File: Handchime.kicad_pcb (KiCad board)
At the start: 4 copper layers, 40.6 x 20.2 mm, 23 parts, among them J1 USB_C_Receptacle_USB2.0_16P, J2 Pins, J3 SWD, SW0 BOOT, SW1 Row 0, Col 0, SW2 Row 0, Col 1, U1 STM32C071GBUx, U2 PRTR5V0U2X, U3 XC6206P332MR-G

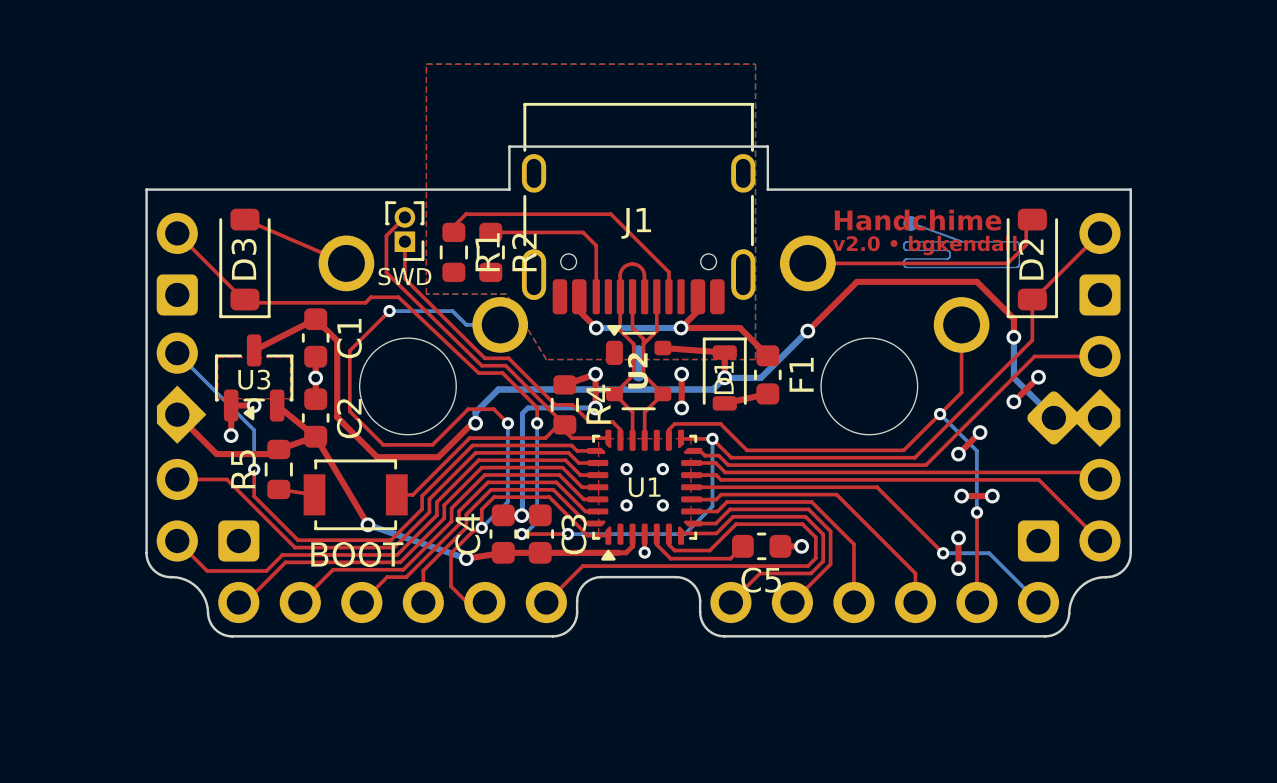
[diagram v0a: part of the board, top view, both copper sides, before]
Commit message: Clean-up edge cuts, tidy routing around NRST
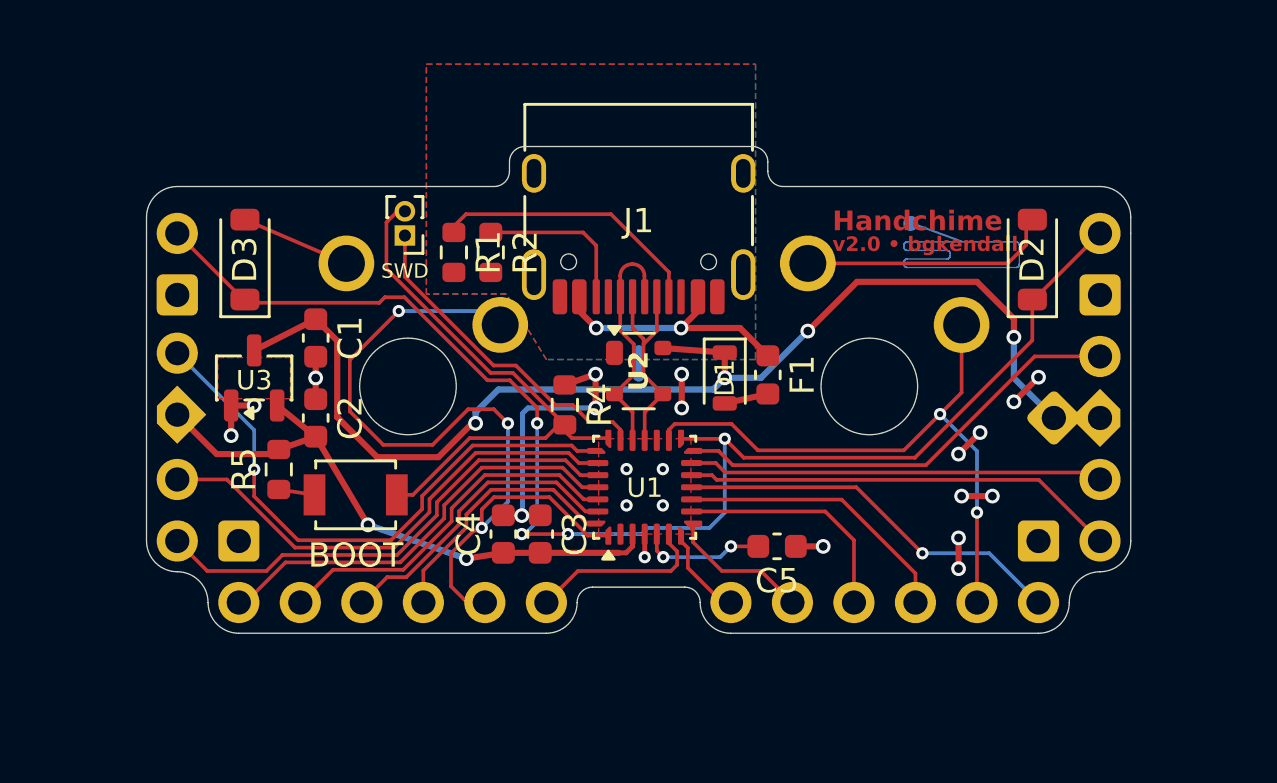
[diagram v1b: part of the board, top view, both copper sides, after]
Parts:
- moved C5 0.64 mm to (158.1, 57.4)
- moved J3 0.25 mm to (142.7, 44.6)
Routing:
- net PA0: track 20.0 -> 7.45 mm
- net PA1: track 12.1 -> 3.82 mm
- net PA2: track 9.89 -> 5.90 mm
- net NRST: track 4.44 -> 5.17 mm, vias 0 -> 2
- net R0: track 57.1 -> 57.8 mm
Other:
- board size 40.6 x 20.2 mm -> 40.6 x 16.5 mm

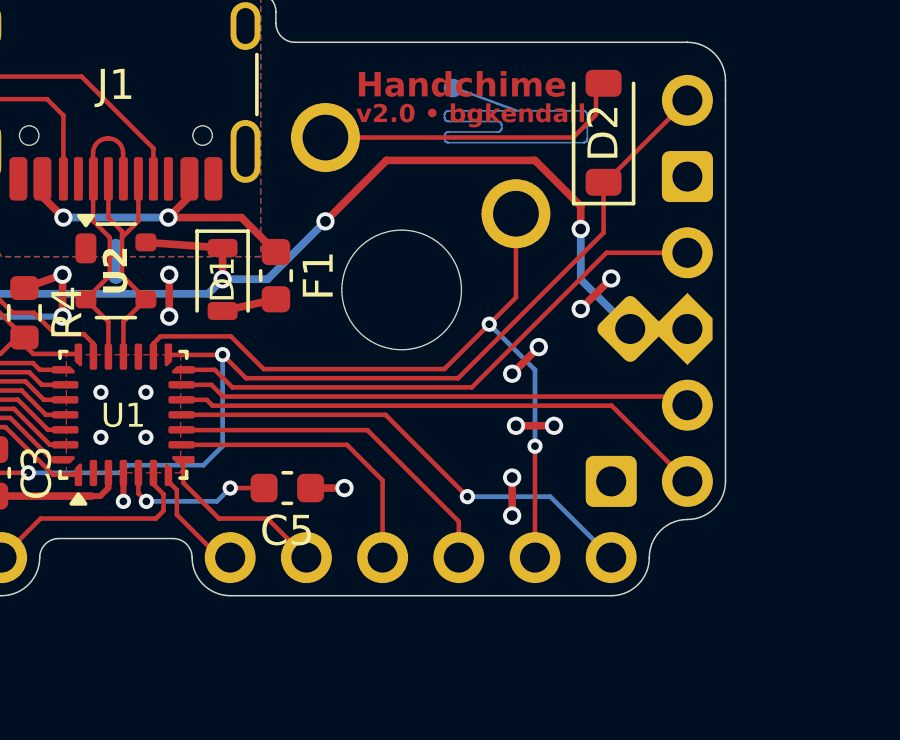
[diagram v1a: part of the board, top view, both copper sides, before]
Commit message: Add RGB pull-up to edge pin 22
PB0 has the following timers available for driving RGB LEDs using PWM:

 * TIM3_CH3
 * TIM1_CH2N
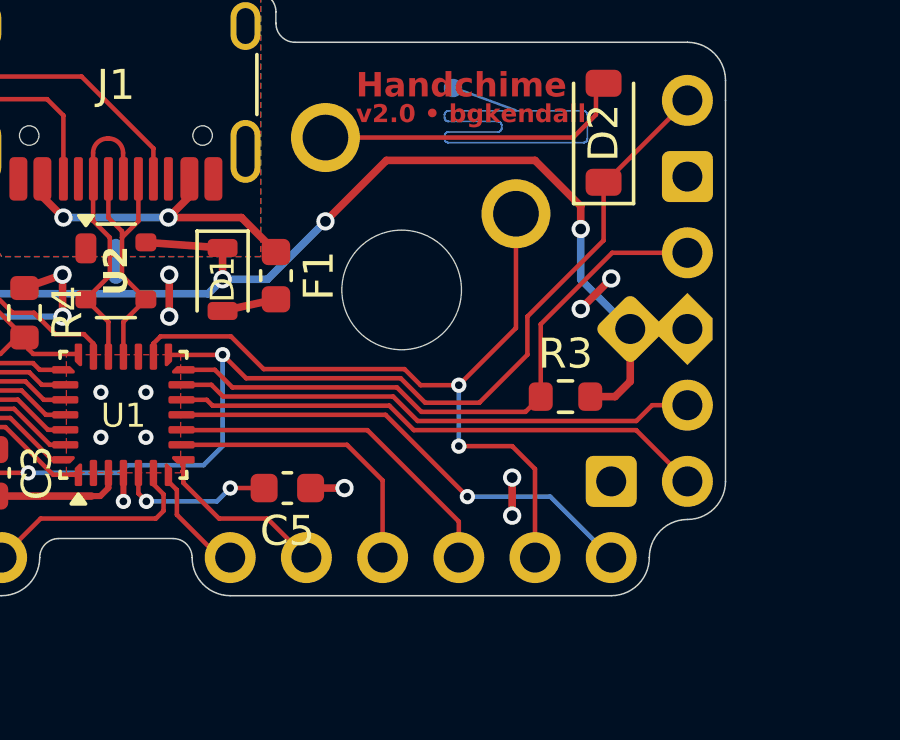
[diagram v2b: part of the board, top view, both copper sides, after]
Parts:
- added R3: 5.1k, Resistor_SMD:R_0603_1608Metric, F.Cu at (167.4, 54.4)
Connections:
- net PB0 renamed RGB
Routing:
- net VCC: track 48.4 -> 51.7 mm
- net GND: track 24.2 -> 21.7 mm, vias 22 -> 18
- net RGB: track 18.9 -> 21.0 mm
- net R0: track 57.8 -> 59.4 mm

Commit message: Minor tweaks around U3
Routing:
- net GND: track 21.7 -> 20.8 mm, vias 18 -> 19
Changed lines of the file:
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@@
-	)
-	(segment
-		(start 136.525 51.5882)
-		(end 135.575001 51.5882)
-		(width 0.254)
-		(layer "F.Cu")
-		(net "GND")
 	)
 	(segment
@@
 	)
 	(via
-		(at 136.525 51.5882)
+		(at 135.448001 50.038)
 		(size 0.6096)
 		(drill 0.3556)
@@
 	(via
 		(at 150.622 51.689)
+		(size 0.6096)
+		(drill 0.3556)
+		(layers "F.Cu" "B.Cu")
+		(net "GND")
+	)
+	(via
+		(at 137.601999 50.038)
 		(size 0.6096)
 		(drill 0.3556)
@@
 	)
 	(segment
-		(start 145.669 51.8668)
-		(end 146.6088 50.927)
-		(width 0.254)
-		(layer "B.Cu")
-		(net "VCC")
-	)
-	(segment
-		(start 146.6088 50.927)
-		(end 155.4734 50.927)
+		(start 155.4099 50.9905)
+		(end 155.956 50.4444)
 		(width 0.254)
 		(layer "B.Cu")
@@
 	)
 	(segment
-		(start 155.4734 50.927)
-		(end 155.956 50.4444)
+		(start 145.669 51.8668)
+		(end 146.5453 50.9905)
 		(width 0.254)
 		(layer "B.Cu")
@@
 		(width 0.254)
 		(layer "B.Cu")
+		(net "VCC")
+	)
+	(segment
+		(start 146.5453 50.9905)
+		(end 155.4099 50.9905)
+		(width 0.254)
+		(layer "B.Cu")

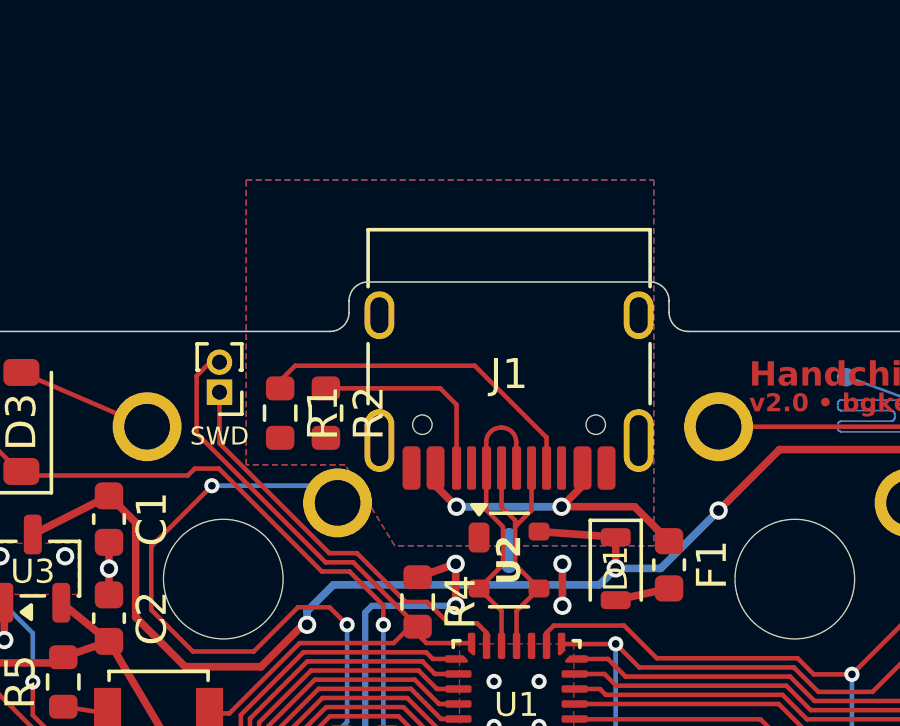
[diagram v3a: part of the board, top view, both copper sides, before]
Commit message: Switch to two-layer stack-up
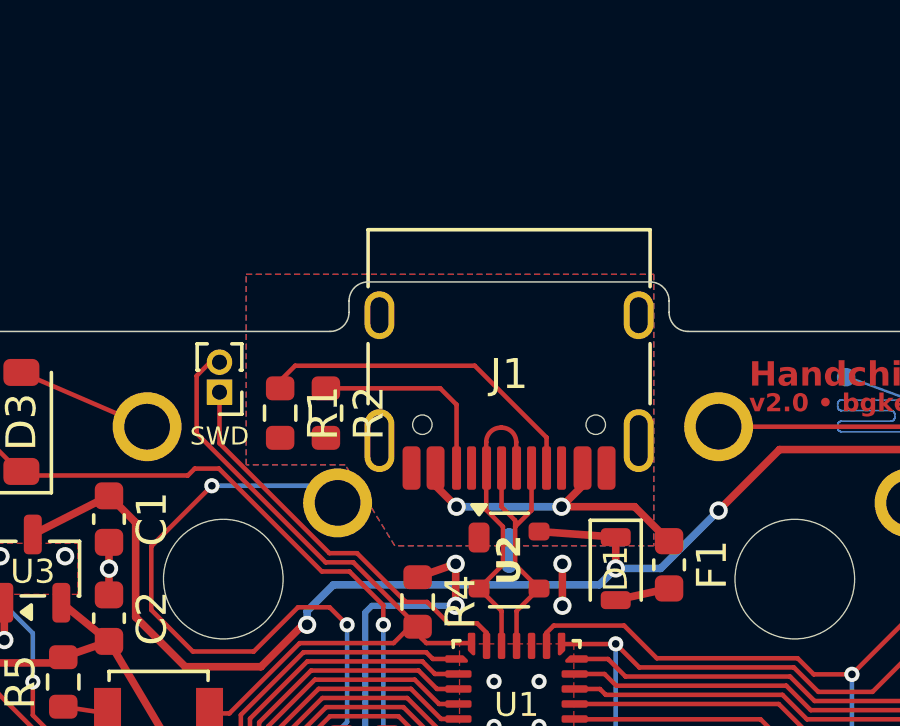
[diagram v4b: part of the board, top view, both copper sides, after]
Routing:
- removed copper zone on In1.Cu, net ISLAND
- removed copper zone on In2.Cu, net ISLAND
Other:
- copper layers 4 -> 2
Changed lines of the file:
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@@
 	(layers
 		(0 "F.Cu" signal)
-		(4 "In1.Cu" power)
-		(6 "In2.Cu" signal)
 		(2 "B.Cu" power)
 		(9 "F.Adhes" user "F.Adhesive")
@@
 			)
 			(layer "dielectric 1"
-				(type "prepreg")
-				(color "FR4 natural")
-				(thickness 0.2104)
-				(material "FR4")
-				(epsilon_r 4.4)
-				(loss_tangent 0.02)
-			)
-			(layer "In1.Cu"
-				(type "copper")
-				(thickness 0.0152)
-			)
-			(layer "dielectric 2"
 				(type "core")
 				(color "FR4 natural")
-				(thickness 1.065)
-				(material "FR4")
-				(epsilon_r 4.6)
-				(loss_tangent 0.02)
-			)
-			(layer "In2.Cu"
-				(type "copper")
-				(thickness 0.0152)
-			)
-			(layer "dielectric 3"
-				(type "prepreg")
-				(color "FR4 natural")
-				(thickness 0.2104)
+				(thickness 1.5162)
 				(material "FR4")
 				(epsilon_r 4.4)
@@
 		(capping no)
 		(filling no)
+		(zone_defaults)
 		(pcbplotparams
 			(layerselection 0x00000000_00000000_55555555_5755f5ff)
@@
 	(zone
 		(net "ISLAND")
-		(layers "F.Cu" "B.Cu" "In1.Cu" "In2.Cu")
+		(layers "F.Cu" "B.Cu")
 		(hatch edge 0.5)
 		(priority 2)
@@
 		(polygon
 			(pts
-				(xy 146.939 46.99) (xy 143.637 46.99) (xy 143.637 37.4967) (xy 157.226 37.4967) (xy 157.226 49.6887)
+				(xy 146.939 46.99) (xy 143.637 46.99) (xy 143.637 40.64) (xy 157.226 40.64) (xy 157.226 49.6887)
 				(xy 148.59 49.6887)
 			)

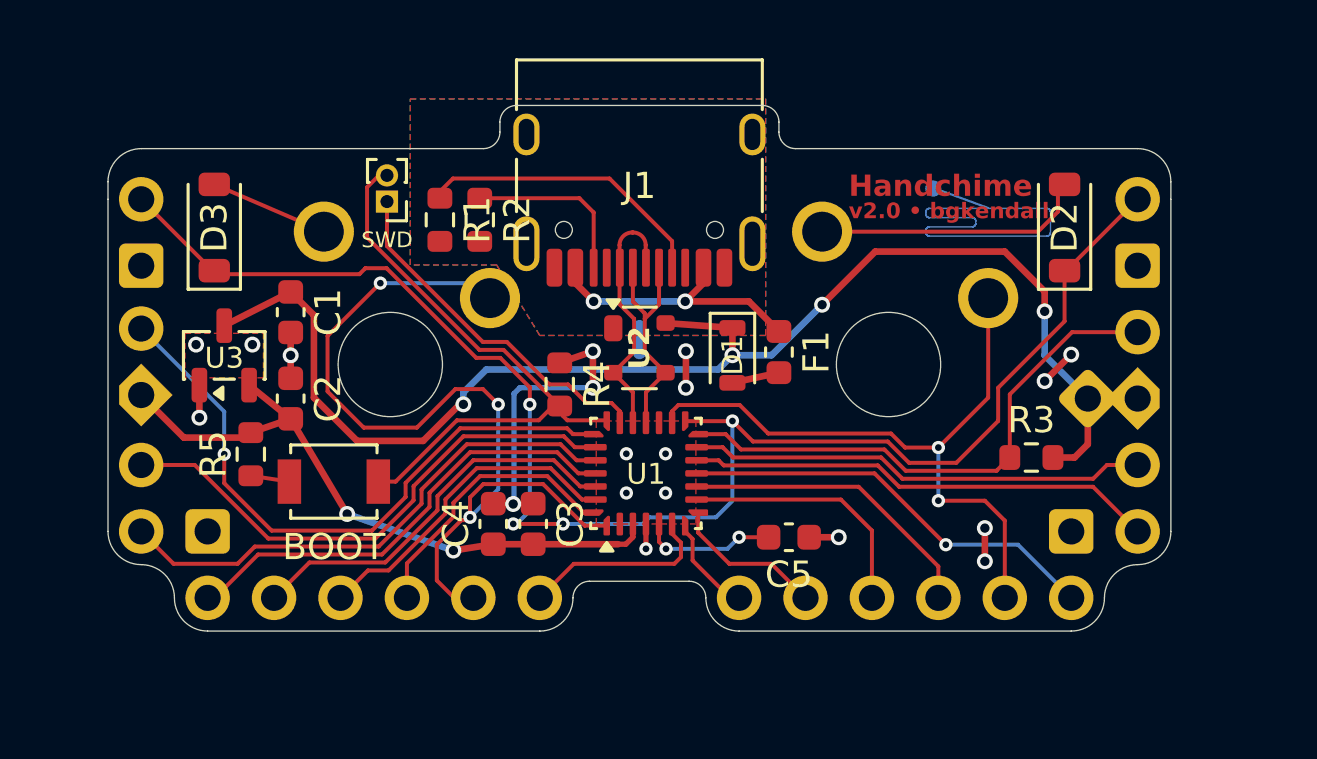
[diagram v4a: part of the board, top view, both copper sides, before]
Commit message: Clean-up silkscreens, tweak routing
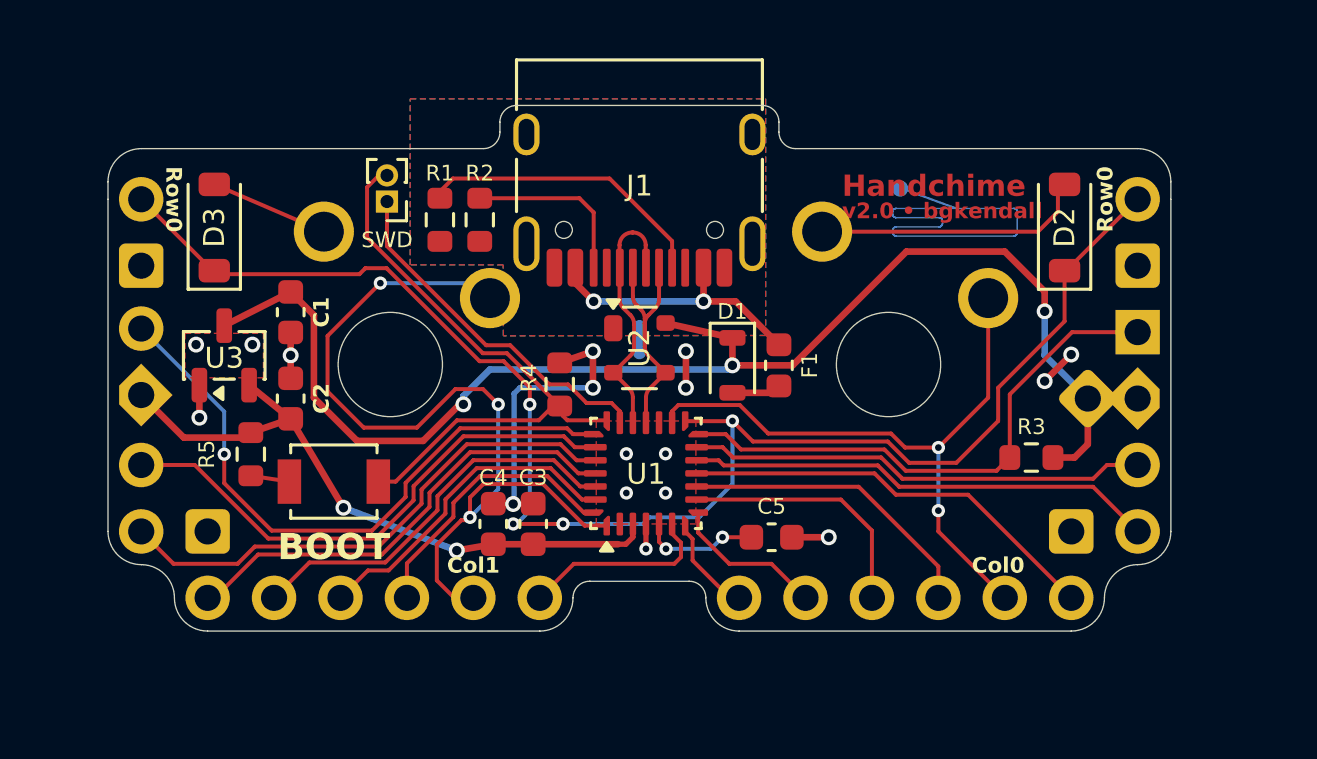
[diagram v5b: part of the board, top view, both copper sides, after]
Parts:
- moved C5 0.66 mm to (157.5, 57.4)
- moved F1 0.51 mm to (157.7, 50.8)
- moved D1 0.38 mm to (156.0, 50.8)
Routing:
- net C0: track 25.7 -> 24.7 mm
- net GND: track 20.8 -> 19.8 mm, vias 19 -> 17
- net NRST: track 5.17 -> 4.51 mm
- net USB-: track 8.94 -> 9.53 mm
- net VCC: track 51.7 -> 51.4 mm, vias 4 -> 3
- net PA5: vias 1 -> 0
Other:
- board text added: "${REVISION} • ${COMPANY}"
- board text added: "${TITLE}"
- board text removed: "Handchime"
- board text removed: "v2.0 • bgkendall"

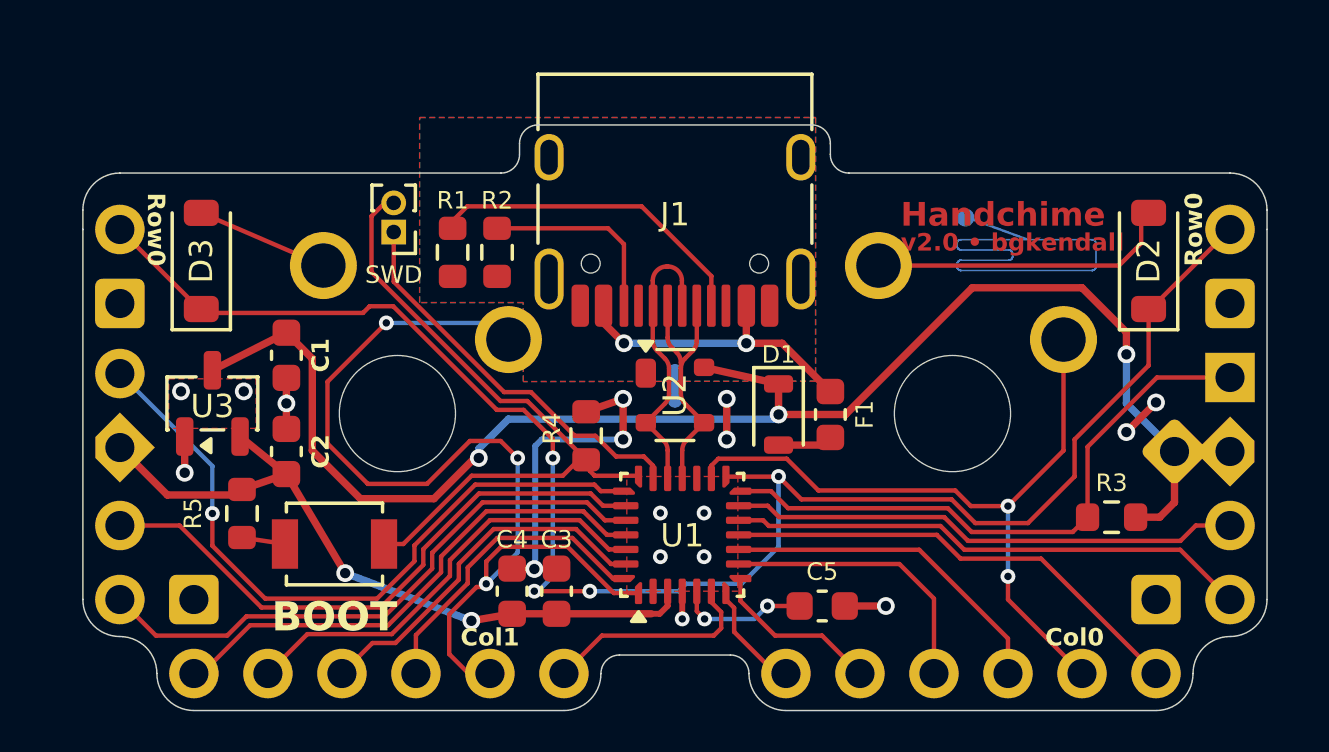
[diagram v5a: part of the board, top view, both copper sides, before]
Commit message: Tweak component placement
Tidy F1 and D1, and swap C3 and C3
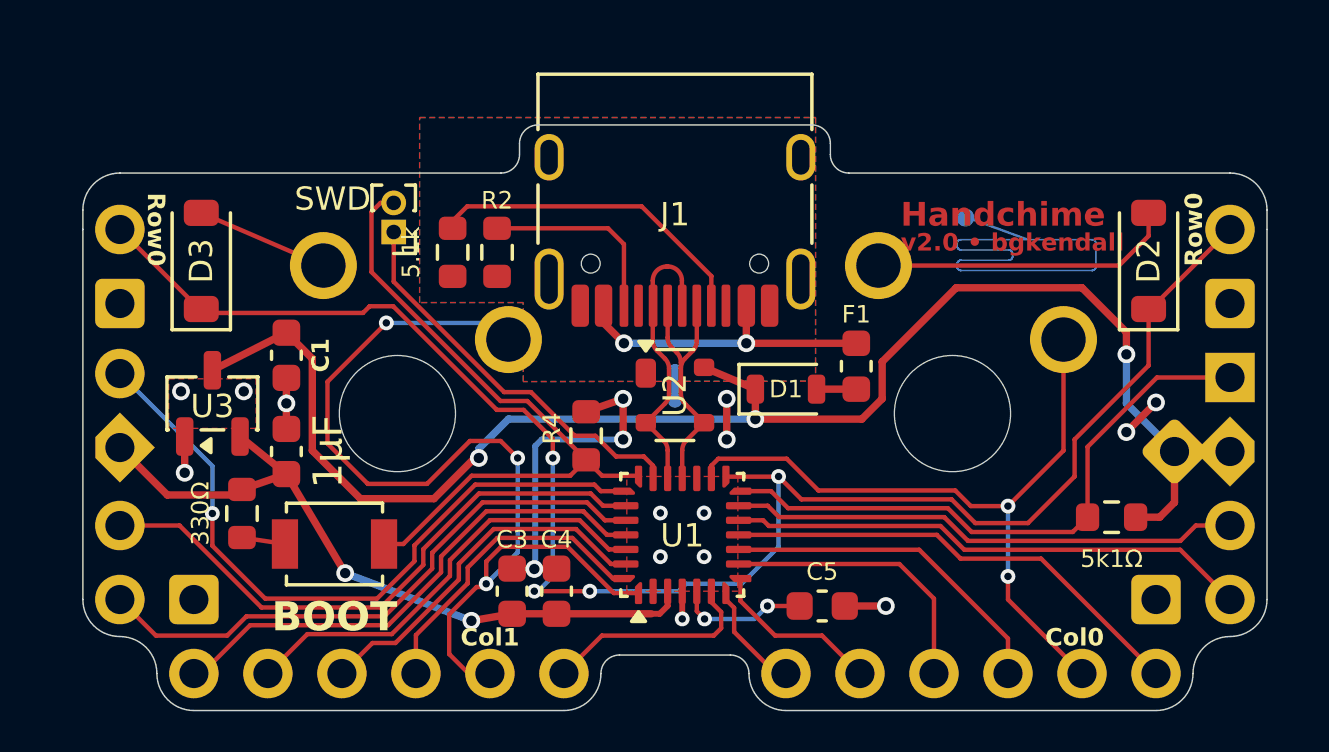
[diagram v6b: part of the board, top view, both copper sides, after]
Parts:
- R3: value 5.1k -> 5k1Ω
- moved F1 1.88 mm to (158.6, 49.2)
- moved C4 1.52 mm to (148.3, 56.9)
- moved C3 1.52 mm to (146.8, 56.9)
- moved D1 0.91 mm to (156.2, 50.0), turned to 0 degrees
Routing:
- net Net-(D1-A): track 1.89 -> 1.36 mm
